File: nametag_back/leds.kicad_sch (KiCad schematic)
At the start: 72 parts, among them Q1 BSS138, Q10 BSS138, Q11 BSS138, Q12 BSS138, Q13 BSS138, Q14 BSS138, Q15 BSS138, Q16 BSS138, Q17 BSS138, Q18 BSS138, Q19 BSS138, Q2 BSS138, Q20 BSS138, Q21 BSS138, Q22 BSS138, Q23 BSS138, Q24 BSS138, Q3 BSS138, Q4 BSS138, Q5 BSS138, Q6 BSS138, Q7 BSS138, Q8 BSS138, Q9 BSS138

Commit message: Finish both pcbs for a two-tier PCB
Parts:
- added D25, D26, D27: LED, LED_SMD:LED_1206_3216Metric, symbol Device:LED
- added Q25, Q26, Q27: BSS138, Package_TO_SOT_SMD:SOT-23, symbol Transistor_FET:BSS138
- added R25, R26, R27: 1k, Resistor_SMD:R_0805_2012Metric, symbol Device:R
- R1, R10, R11, R12, R13, R14, R15, R16, R17, R18, R19, R2, R20, R21, R22, R23, R24, R3, R4, R5, R6, R7, R8, R9: value R -> 1k
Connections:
- net +3V3: now also D25.2 (A), D26.2 (A), D27.2 (A)
- net CTRL: now also Q25.1 (G), Q26.1 (G), Q27.1 (G)
- net GND: now also Q25.2 (S), Q26.2 (S), Q27.2 (S)
- new net: Q27.3 (D), R27.2
- new net: Q25.3 (D), R25.2
- new net: Q26.3 (D), R26.2
- new net: D27.1 (K), R27.1
- new net: D25.1 (K), R25.1
- new net: D26.1 (K), R26.1

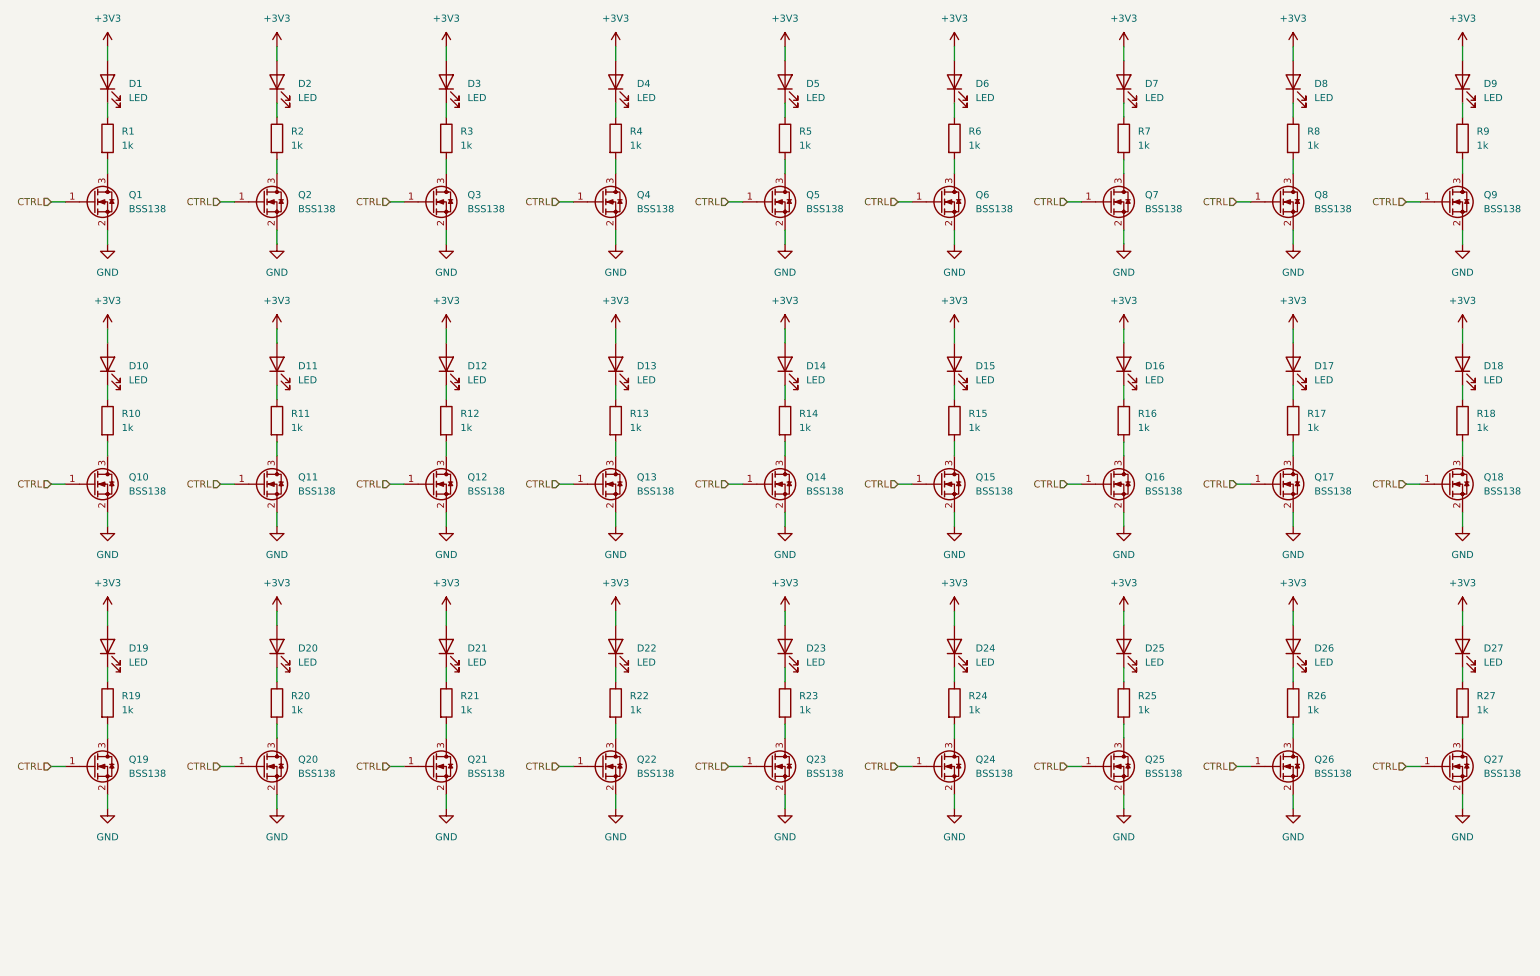
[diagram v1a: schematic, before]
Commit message: Remove all but one low-side mosfets
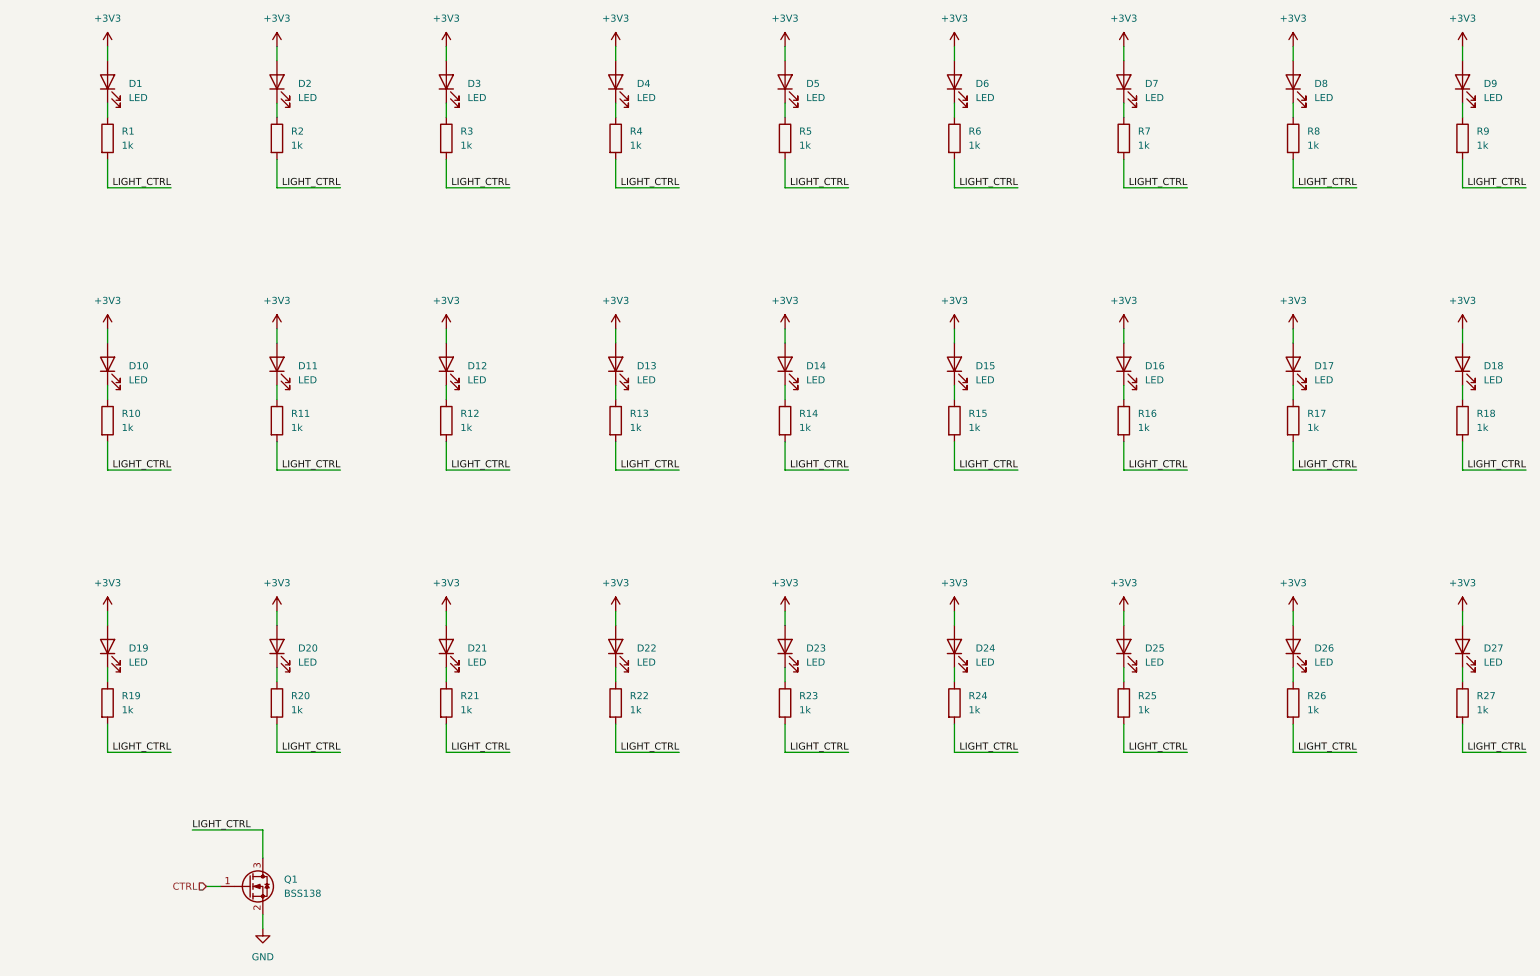
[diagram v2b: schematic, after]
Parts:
- removed Q10, Q11, Q12, Q13, Q14, Q15, Q16, Q17, Q18, Q19, Q2, Q20, Q21, Q22, Q23, Q24, Q25, Q26, Q27, Q3, Q4, Q5, Q6, Q7, Q8, Q9: BSS138, Package_TO_SOT_SMD:SOT-23, symbol Transistor_FET:BSS138
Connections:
- net LIGHT_CTRL: now reaches R21.2
- net LIGHT_CTRL: now also Q1.3 (D), R1.2, R10.2, R11.2, R12.2, R13.2, R14.2, R15.2, R16.2, R17.2, R18.2, R19.2, R2.2, R20.2, R22.2, R23.2, R24.2, R25.2, R26.2, R27.2, R3.2, R4.2, R5.2, R6.2, R7.2, R8.2, R9.2
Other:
- moved on the sheet: Q1

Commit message: Push new fab files
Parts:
- D1, D10, D11, D12, D13, D14, D15, D16, D17, D18, D19, D2, D20, D26, D27, D3, D4, D5, D6, D7, D8, D9: value LED -> YELLOW
- D21, D22, D23, D24, D25: value LED -> GREEN
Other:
- note added: "Low-side Brightness Control"
- note added: "Nametag Backlight"
- note added: "Wrench Backlight"
- company: (none) -> Stan Okrasinski
- title: (none) -> Two-tier nametag - back
- moved on the sheet: D1, D10, D11, D12, D13, D14, D15, D16, D17, D18, D19, D2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
